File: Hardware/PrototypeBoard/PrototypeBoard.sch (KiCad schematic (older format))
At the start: 6 parts

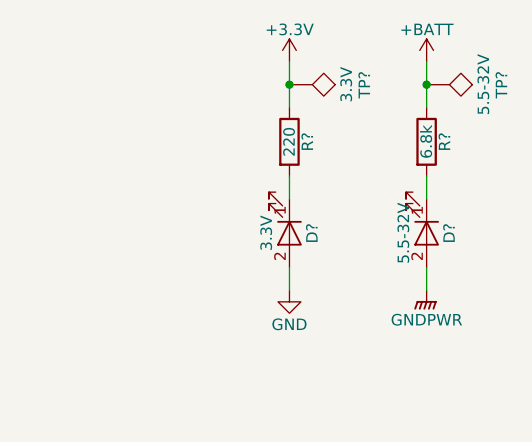
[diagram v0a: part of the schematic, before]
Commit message: Fixed all ERC errors. Added power consumption estimation and other comments. Added links to datasheets. Dimensioned low pass and voltage dividers. Added TVS diodes for protection of voltage rails and ADC inputs. Added fuses. Added Testpoints. Added DC-link capacitors.
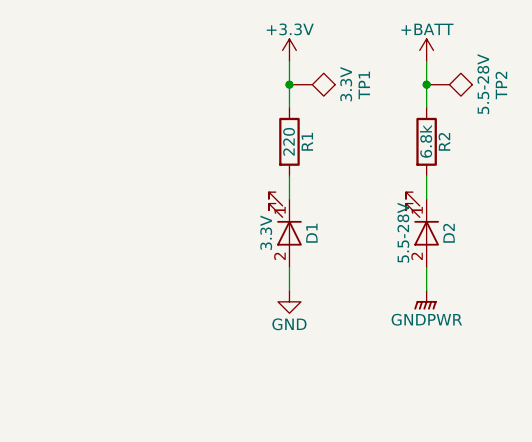
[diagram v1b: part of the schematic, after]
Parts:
- D2: renamed from D?; value 5.5-32V -> 5.5-28V
- TP2: renamed from TP?; value 5.5-32V -> 5.5-28V
- gave numbers to parts that had none: 4
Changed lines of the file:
@@
 	5800 4400 6300 4400
 $Comp
-L +3.3V #PWR?
+L +3.3V #PWR01
 U 1 1 5B002D02
 P 9800 1600
-F 0 "#PWR?" H 9800 1450 50  0001 C CNN
+F 0 "#PWR01" H 9800 1450 50  0001 C CNN
 F 1 "+3.3V" H 9800 1740 50  0000 C CNN
 F 2 "" H 9800 1600 50  0001 C CNN
@@
 $EndComp
 $Comp
-L +BATT #PWR?
+L +BATT #PWR02
 U 1 1 5B002E1E
 P 10400 1600
-F 0 "#PWR?" H 10400 1450 50  0001 C CNN
+F 0 "#PWR02" H 10400 1450 50  0001 C CNN
 F 1 "+BATT" H 10400 1740 50  0000 C CNN
 F 2 "" H 10400 1600 50  0001 C CNN
@@
 $EndComp
 $Comp
-L LED D?
+L LED D1
 U 1 1 5B002F3A
 P 9800 2350
-F 0 "D?" H 9800 2450 50  0000 C CNN
+F 0 "D1" H 9800 2450 50  0000 C CNN
 F 1 "3.3V" H 9800 2250 50  0000 C CNN
 F 2 "" H 9800 2350 50  0001 C CNN
@@
 $EndComp
 $Comp
-L LED D?
+L LED D2
 U 1 1 5B00306C
 P 10400 2350
-F 0 "D?" H 10400 2450 50  0000 C CNN
-F 1 "5.5-32V" H 10400 2250 50  0000 C CNN
+F 0 "D2" H 10400 2450 50  0000 C CNN
+F 1 "5.5-28V" H 10400 2250 50  0000 C CNN
 F 2 "" H 10400 2350 50  0001 C CNN
 F 3 "" H 10400 2350 50  0001 C CNN
@@
 $EndComp
 $Comp
-L GND #PWR?
+L GND #PWR03
 U 1 1 5B0031A0
 P 9800 2600
-F 0 "#PWR?" H 9800 2350 50  0001 C CNN
+F 0 "#PWR03" H 9800 2350 50  0001 C CNN
 F 1 "GND" H 9800 2450 50  0000 C CNN
 F 2 "" H 9800 2600 50  0001 C CNN
@@
 $EndComp
 $Comp
-L GNDPWR #PWR?
+L GNDPWR #PWR04
 U 1 1 5B0032C0
 P 10400 2600
-F 0 "#PWR?" H 10400 2400 50  0001 C CNN
+F 0 "#PWR04" H 10400 2400 50  0001 C CNN
 F 1 "GNDPWR" H 10400 2470 50  0000 C CNN
 F 2 "" H 10400 2550 50  0001 C CNN
@@
 	10400 1600 10400 1800
 $Comp
-L TEST TP?
+L TEST TP2
 U 1 1 5B003DB5
 P 10400 1700
-F 0 "TP?" H 10400 2000 50  0000 C BNN
-F 1 "5.5-32V" H 10400 1950 50  0000 C CNN
+F 0 "TP2" H 10400 2000 50  0000 C BNN
+F 1 "5.5-28V" H 10400 1950 50  0000 C CNN
 F 2 "" H 10400 1700 50  0001 C CNN
 F 3 "" H 10400 1700 50  0001 C CNN
@@
 $EndComp
 $Comp
-L TEST TP?
+L TEST TP1
 U 1 1 5B003EE3
 P 9800 1700
-F 0 "TP?" H 9800 2000 50  0000 C BNN
+F 0 "TP1" H 9800 2000 50  0000 C BNN
 F 1 "3.3V" H 9800 1950 50  0000 C CNN
 F 2 "" H 9800 1700 50  0001 C CNN
@@
 Connection ~ 9800 1700
 $Comp
-L R R?
+L R R1
 U 1 1 5AFEBD88
 P 9800 1950
-F 0 "R?" V 9880 1950 50  0000 C CNN
+F 0 "R1" V 9880 1950 50  0000 C CNN
 F 1 "220" V 9800 1950 50  0000 C CNN
 F 2 "" V 9730 1950 50  0001 C CNN
@@
 $EndComp
 $Comp
-L R R?
+L R R2
 U 1 1 5AFEC09B
 P 10400 1950
-F 0 "R?" V 10480 1950 50  0000 C CNN
+F 0 "R2" V 10480 1950 50  0000 C CNN
 F 1 "6.8k" V 10400 1950 50  0000 C CNN
 F 2 "" V 10330 1950 50  0001 C CNN

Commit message: forgot files
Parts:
- D1, D2: footprint (none) -> LEDs:LED_0805_HandSoldering
- R1, R2: footprint (none) -> Resistors_SMD:R_0805_HandSoldering
- TP1, TP2: footprint (none) -> Measurement_Points:Measurement_Point_Round-TH_Big
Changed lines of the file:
@@
 F 0 "D1" H 9800 2450 50  0000 C CNN
 F 1 "3.3V" H 9800 2250 50  0000 C CNN
-F 2 "" H 9800 2350 50  0001 C CNN
+F 2 "LEDs:LED_0805_HandSoldering" H 9800 2350 50  0001 C CNN
 F 3 "" H 9800 2350 50  0001 C CNN
 	1    9800 2350
@@
 F 0 "D2" H 10400 2450 50  0000 C CNN
 F 1 "5.5-28V" H 10400 2250 50  0000 C CNN
-F 2 "" H 10400 2350 50  0001 C CNN
+F 2 "LEDs:LED_0805_HandSoldering" H 10400 2350 50  0001 C CNN
 F 3 "" H 10400 2350 50  0001 C CNN
 	1    10400 2350
@@
 F 0 "TP2" H 10400 2000 50  0000 C BNN
 F 1 "5.5-28V" H 10400 1950 50  0000 C CNN
-F 2 "" H 10400 1700 50  0001 C CNN
+F 2 "Measurement_Points:Measurement_Point_Round-TH_Big" H 10400 1700 50  0001 C CNN
 F 3 "" H 10400 1700 50  0001 C CNN
 	1    10400 1700
@@
 F 0 "TP1" H 9800 2000 50  0000 C BNN
 F 1 "3.3V" H 9800 1950 50  0000 C CNN
-F 2 "" H 9800 1700 50  0001 C CNN
+F 2 "Measurement_Points:Measurement_Point_Round-TH_Big" H 9800 1700 50  0001 C CNN
 F 3 "" H 9800 1700 50  0001 C CNN
 	1    9800 1700
@@
 F 0 "R1" V 9880 1950 50  0000 C CNN
 F 1 "220" V 9800 1950 50  0000 C CNN
-F 2 "" V 9730 1950 50  0001 C CNN
+F 2 "Resistors_SMD:R_0805_HandSoldering" V 9730 1950 50  0001 C CNN
 F 3 "" H 9800 1950 50  0001 C CNN
 	1    9800 1950
@@
 F 0 "R2" V 10480 1950 50  0000 C CNN
 F 1 "6.8k" V 10400 1950 50  0000 C CNN
-F 2 "" V 10330 1950 50  0001 C CNN
+F 2 "Resistors_SMD:R_0805_HandSoldering" V 10330 1950 50  0001 C CNN
 F 3 "" H 10400 1950 50  0001 C CNN
 	1    10400 1950

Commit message: minor progress in layout
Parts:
- TP1, TP2: footprint Measurement_Points:Measurement_Point_Round-TH_Big -> Measurement_Points:Measurement_Point_Round-SMD-Pad_Small
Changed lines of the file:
@@
 F 0 "TP2" H 10400 2000 50  0000 C BNN
 F 1 "5.5-28V" H 10400 1950 50  0000 C CNN
-F 2 "Measurement_Points:Measurement_Point_Round-TH_Big" H 10400 1700 50  0001 C CNN
+F 2 "Measurement_Points:Measurement_Point_Round-SMD-Pad_Small" H 10400 1700 50  0001 C CNN
 F 3 "" H 10400 1700 50  0001 C CNN
 	1    10400 1700
@@
 F 0 "TP1" H 9800 2000 50  0000 C BNN
 F 1 "3.3V" H 9800 1950 50  0000 C CNN
-F 2 "Measurement_Points:Measurement_Point_Round-TH_Big" H 9800 1700 50  0001 C CNN
+F 2 "Measurement_Points:Measurement_Point_Round-SMD-Pad_Small" H 9800 1700 50  0001 C CNN
 F 3 "" H 9800 1700 50  0001 C CNN
 	1    9800 1700

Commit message: more layout and some changes to schematic
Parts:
- TP1, TP2: footprint Measurement_Points:Measurement_Point_Round-SMD-Pad_Small -> Pin_Headers:Pin_Header_Straight_1x01_Pitch2.00mm
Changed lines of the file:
@@
 F 0 "TP2" H 10400 2000 50  0000 C BNN
 F 1 "5.5-28V" H 10400 1950 50  0000 C CNN
-F 2 "Measurement_Points:Measurement_Point_Round-SMD-Pad_Small" H 10400 1700 50  0001 C CNN
+F 2 "Pin_Headers:Pin_Header_Straight_1x01_Pitch2.00mm" H 10400 1700 50  0001 C CNN
 F 3 "" H 10400 1700 50  0001 C CNN
 	1    10400 1700
@@
 F 0 "TP1" H 9800 2000 50  0000 C BNN
 F 1 "3.3V" H 9800 1950 50  0000 C CNN
-F 2 "Measurement_Points:Measurement_Point_Round-SMD-Pad_Small" H 9800 1700 50  0001 C CNN
+F 2 "Pin_Headers:Pin_Header_Straight_1x01_Pitch2.00mm" H 9800 1700 50  0001 C CNN
 F 3 "" H 9800 1700 50  0001 C CNN
 	1    9800 1700

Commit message: Migrated to kicad 5
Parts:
- D1, D2: symbol LED -> Device:LED
- R1, R2: symbol R -> Device:R
- TP1, TP2: symbol TEST -> PrototypeBoard-rescue:TEST
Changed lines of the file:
@@
-EESchema Schematic File Version 2
-LIBS:power
-LIBS:device
-LIBS:switches
-LIBS:relays
-LIBS:motors
-LIBS:transistors
-LIBS:conn
-LIBS:linear
-LIBS:regul
-LIBS:74xx
-LIBS:cmos4000
-LIBS:adc-dac
-LIBS:memory
-LIBS:xilinx
-LIBS:microcontrollers
-LIBS:dsp
-LIBS:microchip
-LIBS:analog_switches
-LIBS:motorola
-LIBS:texas
-LIBS:intel
-LIBS:audio
-LIBS:interface
-LIBS:digital-audio
-LIBS:philips
-LIBS:display
-LIBS:cypress
-LIBS:siliconi
-LIBS:opto
-LIBS:atmel
-LIBS:contrib
-LIBS:valves
+EESchema Schematic File Version 4
 LIBS:PrototypeBoard-cache
-EELAYER 25 0
+EELAYER 26 0
 EELAYER END
 $Descr A4 11693 8268
@@
 	5800 4400 6300 4400
 $Comp
-L +3.3V #PWR01
+L power:+3.3V #PWR01
 U 1 1 5B002D02
 P 9800 1600
@@
 $EndComp
 $Comp
-L +BATT #PWR02
+L power:+BATT #PWR02
 U 1 1 5B002E1E
 P 10400 1600
@@
 $EndComp
 $Comp
-L LED D1
+L Device:LED D1
 U 1 1 5B002F3A
 P 9800 2350
@@
 $EndComp
 $Comp
-L LED D2
+L Device:LED D2
 U 1 1 5B00306C
 P 10400 2350
@@
 $EndComp
 $Comp
-L GND #PWR03
+L power:GND #PWR03
 U 1 1 5B0031A0
 P 9800 2600
@@
 $EndComp
 $Comp
-L GNDPWR #PWR04
+L PrototypeBoard-rescue:GNDPWR #PWR04
 U 1 1 5B0032C0
 P 10400 2600
@@
 	10400 2500 10400 2600
 Wire Wire Line
-	9800 1600 9800 1800
-Wire Wire Line
-	10400 1600 10400 1800
-$Comp
-L TEST TP2
+	9800 1600 9800 1700
+Wire Wire Line
+	10400 1600 10400 1700
+$Comp
+L PrototypeBoard-rescue:TEST TP2
 U 1 1 5B003DB5
 P 10400 1700
@@
 $EndComp
 $Comp
-L TEST TP1
+L PrototypeBoard-rescue:TEST TP1
 U 1 1 5B003EE3
 P 9800 1700
@@
 Connection ~ 9800 1700
 $Comp
-L R R1
+L Device:R R1
 U 1 1 5AFEBD88
 P 9800 1950
@@
 $EndComp
 $Comp
-L R R2
+L Device:R R2
 U 1 1 5AFEC09B
 P 10400 1950
@@
 Wire Wire Line
 	10400 2100 10400 2200
+Wire Wire Line
+	10400 1700 10400 1800
+Wire Wire Line
+	9800 1700 9800 1800
 $EndSCHEMATC

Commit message: New, much bigger pcb layout, changes to connection PGND <-> GND
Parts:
- added MH1, MH2, MH3, MH4: MountingHole_Pad, Mounting_Holes:MountingHole_3.2mm_M3_Pad_Via, symbol Mechanical:MountingHole_Pad
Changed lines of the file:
@@
 	5800 4400 6300 4400
 $Comp
-L power:+3.3V #PWR01
+L power:+3.3V #PWR03
 U 1 1 5B002D02
 P 9800 1600
-F 0 "#PWR01" H 9800 1450 50  0001 C CNN
+F 0 "#PWR03" H 9800 1450 50  0001 C CNN
 F 1 "+3.3V" H 9800 1740 50  0000 C CNN
 F 2 "" H 9800 1600 50  0001 C CNN
@@
 $EndComp
 $Comp
-L power:+BATT #PWR02
+L power:+BATT #PWR07
 U 1 1 5B002E1E
 P 10400 1600
-F 0 "#PWR02" H 10400 1450 50  0001 C CNN
+F 0 "#PWR07" H 10400 1450 50  0001 C CNN
 F 1 "+BATT" H 10400 1740 50  0000 C CNN
 F 2 "" H 10400 1600 50  0001 C CNN
@@
 $EndComp
 $Comp
-L power:GND #PWR03
+L power:GND #PWR04
 U 1 1 5B0031A0
 P 9800 2600
-F 0 "#PWR03" H 9800 2350 50  0001 C CNN
+F 0 "#PWR04" H 9800 2350 50  0001 C CNN
 F 1 "GND" H 9800 2450 50  0000 C CNN
 F 2 "" H 9800 2600 50  0001 C CNN
@@
 $EndComp
 $Comp
-L PrototypeBoard-rescue:GNDPWR #PWR04
+L PrototypeBoard-rescue:GNDPWR #PWR08
 U 1 1 5B0032C0
 P 10400 2600
-F 0 "#PWR04" H 10400 2400 50  0001 C CNN
+F 0 "#PWR08" H 10400 2400 50  0001 C CNN
 F 1 "GNDPWR" H 10400 2470 50  0000 C CNN
 F 2 "" H 10400 2550 50  0001 C CNN
@@
 Wire Wire Line
 	9800 1700 9800 1800
+$Comp
+L Mechanical:MountingHole_Pad MH?
+U 1 1 5B88C317
+P 9000 4500
+AR Path="/56D57CF9/5B88C317" Ref="MH?"  Part="1"
+AR Path="/5B88C317" Ref="MH1"  Part="1"
+F 0 "MH1" H 9100 4551 50  0000 L CNN
+F 1 "MountingHole_Pad" H 9100 4460 50  0000 L CNN
+F 2 "Mounting_Holes:MountingHole_3.2mm_M3_Pad_Via" H 9000 4500 50  0001 C CNN
+F 3 "~" H 9000 4500 50  0001 C CNN
+	1    9000 4500
+	1    0    0    -1
+$EndComp
+$Comp
+L Mechanical:MountingHole_Pad MH?
+U 1 1 5B88C31E
+P 10100 4500
+AR Path="/56D57CF9/5B88C31E" Ref="MH?"  Part="1"
+AR Path="/5B88C31E" Ref="MH3"  Part="1"
+F 0 "MH3" H 10200 4551 50  0000 L CNN
+F 1 "MountingHole_Pad" H 10200 4460 50  0000 L CNN
+F 2 "Mounting_Holes:MountingHole_3.2mm_M3_Pad_Via" H 10100 4500 50  0001 C CNN
+F 3 "~" H 10100 4500 50  0001 C CNN
+	1    10100 4500
+	1    0    0    -1
+$EndComp
+$Comp
+L Mechanical:MountingHole_Pad MH?
+U 1 1 5B88C325
+P 9000 5100
+AR Path="/56D57CF9/5B88C325" Ref="MH?"  Part="1"
+AR Path="/5B88C325" Ref="MH2"  Part="1"
+F 0 "MH2" H 9100 5151 50  0000 L CNN
+F 1 "MountingHole_Pad" H 9100 5060 50  0000 L CNN
+F 2 "Mounting_Holes:MountingHole_3.2mm_M3_Pad_Via" H 9000 5100 50  0001 C CNN
+F 3 "~" H 9000 5100 50  0001 C CNN
+	1    9000 5100
+	1    0    0    -1
+$EndComp
+$Comp
+L Mechanical:MountingHole_Pad MH?
+U 1 1 5B88C32C
+P 10100 5100
+AR Path="/56D57CF9/5B88C32C" Ref="MH?"  Part="1"
+AR Path="/5B88C32C" Ref="MH4"  Part="1"
+F 0 "MH4" H 10200 5151 50  0000 L CNN
+F 1 "MountingHole_Pad" H 10200 5060 50  0000 L CNN
+F 2 "Mounting_Holes:MountingHole_3.2mm_M3_Pad_Via" H 10100 5100 50  0001 C CNN
+F 3 "~" H 10100 5100 50  0001 C CNN
+	1    10100 5100
+	1    0    0    -1
+$EndComp
+$Comp
+L PrototypeBoard-rescue:GNDPWR #PWR?
+U 1 1 5B88FB48
+P 9000 5200
+AR Path="/5AFD76B5/5B88FB48" Ref="#PWR?"  Part="1"
+AR Path="/5B88FB48" Ref="#PWR02"  Part="1"
+F 0 "#PWR02" H 9000 5000 50  0001 C CNN
+F 1 "GNDPWR" H 9000 5070 50  0000 C CNN
+F 2 "" H 9000 5150 50  0001 C CNN
+F 3 "" H 9000 5150 50  0001 C CNN
+	1    9000 5200
+	1    0    0    -1
+$EndComp
+$Comp
+L PrototypeBoard-rescue:GNDPWR #PWR?
+U 1 1 5B88FE88
+P 9000 4600
+AR Path="/5AFD76B5/5B88FE88" Ref="#PWR?"  Part="1"
+AR Path="/5B88FE88" Ref="#PWR01"  Part="1"
+F 0 "#PWR01" H 9000 4400 50  0001 C CNN
+F 1 "GNDPWR" H 9000 4470 50  0000 C CNN
+F 2 "" H 9000 4550 50  0001 C CNN
+F 3 "" H 9000 4550 50  0001 C CNN
+	1    9000 4600
+	1    0    0    -1
+$EndComp
+$Comp
+L PrototypeBoard-rescue:GNDPWR #PWR?
+U 1 1 5B88FEA7
+P 10100 4600
+AR Path="/5AFD76B5/5B88FEA7" Ref="#PWR?"  Part="1"
+AR Path="/5B88FEA7" Ref="#PWR05"  Part="1"
+F 0 "#PWR05" H 10100 4400 50  0001 C CNN
+F 1 "GNDPWR" H 10100 4470 50  0000 C CNN
+F 2 "" H 10100 4550 50  0001 C CNN
+F 3 "" H 10100 4550 50  0001 C CNN
+	1    10100 4600
+	1    0    0    -1
+$EndComp
+$Comp
+L PrototypeBoard-rescue:GNDPWR #PWR?
+U 1 1 5B88FEC6
+P 10100 5200
+AR Path="/5AFD76B5/5B88FEC6" Ref="#PWR?"  Part="1"
+AR Path="/5B88FEC6" Ref="#PWR06"  Part="1"
+F 0 "#PWR06" H 10100 5000 50  0001 C CNN
+F 1 "GNDPWR" H 10100 5070 50  0000 C CNN
+F 2 "" H 10100 5150 50  0001 C CNN
+F 3 "" H 10100 5150 50  0001 C CNN
+	1    10100 5200
+	1    0    0    -1
+$EndComp
 $EndSCHEMATC

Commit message: continued to work on new layout
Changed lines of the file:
@@
 $EndComp
 $Comp
-L PrototypeBoard-rescue:GNDPWR #PWR?
-U 1 1 5B88FB48
-P 9000 5200
-AR Path="/5AFD76B5/5B88FB48" Ref="#PWR?"  Part="1"
-AR Path="/5B88FB48" Ref="#PWR02"  Part="1"
-F 0 "#PWR02" H 9000 5000 50  0001 C CNN
-F 1 "GNDPWR" H 9000 5070 50  0000 C CNN
-F 2 "" H 9000 5150 50  0001 C CNN
-F 3 "" H 9000 5150 50  0001 C CNN
-	1    9000 5200
-	1    0    0    -1
-$EndComp
-$Comp
-L PrototypeBoard-rescue:GNDPWR #PWR?
-U 1 1 5B88FE88
+L power:GND #PWR?
+U 1 1 5B8A531B
 P 9000 4600
-AR Path="/5AFD76B5/5B88FE88" Ref="#PWR?"  Part="1"
-AR Path="/5B88FE88" Ref="#PWR01"  Part="1"
-F 0 "#PWR01" H 9000 4400 50  0001 C CNN
-F 1 "GNDPWR" H 9000 4470 50  0000 C CNN
-F 2 "" H 9000 4550 50  0001 C CNN
-F 3 "" H 9000 4550 50  0001 C CNN
+F 0 "#PWR?" H 9000 4350 50  0001 C CNN
+F 1 "GND" H 9000 4450 50  0000 C CNN
+F 2 "" H 9000 4600 50  0001 C CNN
+F 3 "" H 9000 4600 50  0001 C CNN
 	1    9000 4600
 	1    0    0    -1
 $EndComp
 $Comp
-L PrototypeBoard-rescue:GNDPWR #PWR?
-U 1 1 5B88FEA7
+L power:GND #PWR?
+U 1 1 5B8A53AC
 P 10100 4600
-AR Path="/5AFD76B5/5B88FEA7" Ref="#PWR?"  Part="1"
-AR Path="/5B88FEA7" Ref="#PWR05"  Part="1"
-F 0 "#PWR05" H 10100 4400 50  0001 C CNN
-F 1 "GNDPWR" H 10100 4470 50  0000 C CNN
-F 2 "" H 10100 4550 50  0001 C CNN
-F 3 "" H 10100 4550 50  0001 C CNN
+F 0 "#PWR?" H 10100 4350 50  0001 C CNN
+F 1 "GND" H 10100 4450 50  0000 C CNN
+F 2 "" H 10100 4600 50  0001 C CNN
+F 3 "" H 10100 4600 50  0001 C CNN
 	1    10100 4600
 	1    0    0    -1
 $EndComp
 $Comp
-L PrototypeBoard-rescue:GNDPWR #PWR?
-U 1 1 5B88FEC6
+L power:GND #PWR?
+U 1 1 5B8A53CB
 P 10100 5200
-AR Path="/5AFD76B5/5B88FEC6" Ref="#PWR?"  Part="1"
-AR Path="/5B88FEC6" Ref="#PWR06"  Part="1"
-F 0 "#PWR06" H 10100 5000 50  0001 C CNN
-F 1 "GNDPWR" H 10100 5070 50  0000 C CNN
-F 2 "" H 10100 5150 50  0001 C CNN
-F 3 "" H 10100 5150 50  0001 C CNN
+F 0 "#PWR?" H 10100 4950 50  0001 C CNN
+F 1 "GND" H 10100 5050 50  0000 C CNN
+F 2 "" H 10100 5200 50  0001 C CNN
+F 3 "" H 10100 5200 50  0001 C CNN
 	1    10100 5200
 	1    0    0    -1
 $EndComp
+$Comp
+L power:GND #PWR?
+U 1 1 5B8A53EA
+P 9000 5200
+F 0 "#PWR?" H 9000 4950 50  0001 C CNN
+F 1 "GND" H 9000 5050 50  0000 C CNN
+F 2 "" H 9000 5200 50  0001 C CNN
+F 3 "" H 9000 5200 50  0001 C CNN
+	1    9000 5200
+	1    0    0    -1
+$EndComp
